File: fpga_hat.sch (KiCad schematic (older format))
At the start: 42 parts, among them IC1 ADV7125, IC3 CS4334, J0 0R, J1 0R, U1 AS6C4008-55PCN, U2 AS6C4008-55PCN, U7 Conn_02x32_Odd_Even, U8 Conn_02x32_Odd_Even

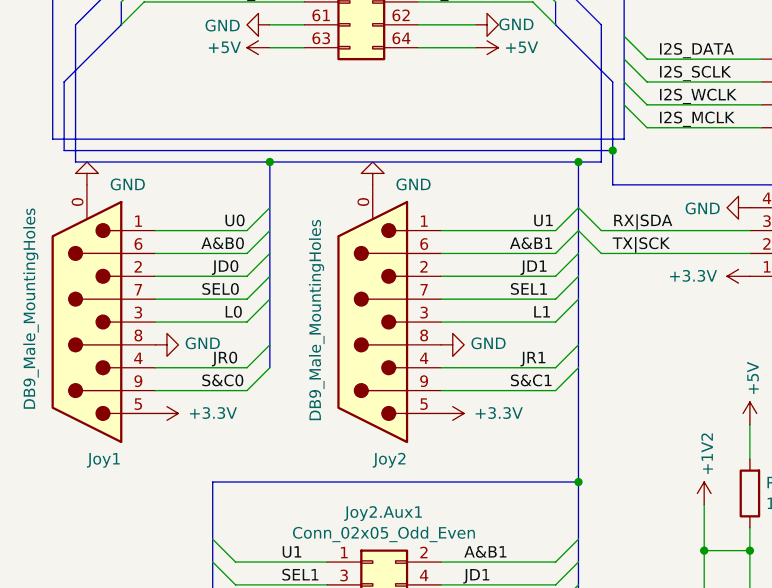
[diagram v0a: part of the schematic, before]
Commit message: Fixed gamepad port routing
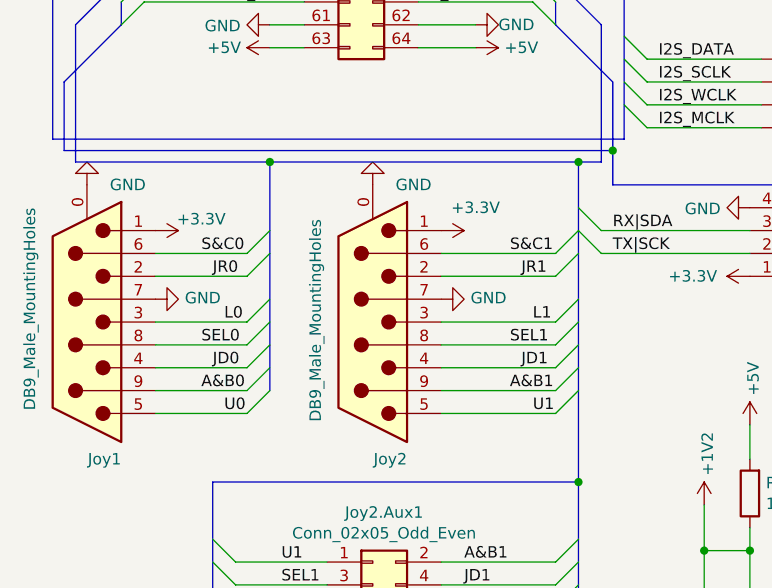
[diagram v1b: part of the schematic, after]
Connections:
- net +3V3: now also Joy1.1, Joy2.1; no longer Joy1.5, Joy2.5
- net A&B0: now also Joy1.9; no longer Joy1.6
- net A&B1: now also Joy2.9; no longer Joy2.6
- net GND: now also Joy1.7, Joy2.7; no longer Joy1.8, Joy2.8
- net JD0: now also Joy1.4; no longer Joy1.2
- net JD1: now also Joy2.4; no longer Joy2.2
- net JR0: now also Joy1.2; no longer Joy1.4
- net JR1: now also Joy2.2; no longer Joy2.4
- net S&C0: now also Joy1.6; no longer Joy1.9
- net S&C1: now also Joy2.6; no longer Joy2.9
- net SEL0: now also Joy1.8; no longer Joy1.7
- net SEL1: now also Joy2.8; no longer Joy2.7
- net U0: now also Joy1.5; no longer Joy1.1
- net U1: now also Joy2.5; no longer Joy2.1
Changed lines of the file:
@@
 Wire Wire Line
 	2300 4900 2550 4900
-$Comp
-L Connector:DB9_Male_MountingHoles Joy2
-U 1 1 6186E5CE
-P 2100 6200
-F 0 "Joy2" H 1950 6800 50  0000 L CNN
-F 1 "DB9_Male_MountingHoles" V 2350 5750 50  0000 L CNN
-F 2 "Connector_Dsub:DSUB-9_Female_Horizontal_P2.77x2.84mm_EdgePinOffset4.94mm_Housed_MountingHolesOffset7.48mm" H 2100 6200 50  0001 C CNN
-F 3 " ~" H 2100 6200 50  0001 C CNN
-	1    2100 6200
-	-1   0    0    1
-$EndComp
-Entry Wire Line
-	1550 5800 1650 5700
 Entry Wire Line
 	1550 5900 1650 5800
@@
 	1550 6000 1650 5900
 Entry Wire Line
-	1550 6100 1650 6000
+	1550 6300 1650 6200
 Entry Wire Line
 	1550 6200 1650 6100
@@
 	2900 6200 3000 6100
 Entry Wire Line
-	2900 6100 3000 6000
+	2900 6300 3000 6200
 Entry Wire Line
 	2900 6000 3000 5900
@@
 	2900 5900 3000 5800
 Entry Wire Line
-	2900 5800 3000 5700
-Wire Wire Line
-	1150 5800 1550 5800
+	2900 6600 3000 6500
 Wire Wire Line
 	1150 5900 1550 5900
@@
 	1150 6000 1550 6000
 Wire Wire Line
-	1150 6100 1550 6100
-Wire Wire Line
 	1150 6400 1550 6400
 Wire Wire Line
@@
 	2400 6200 2900 6200
 Wire Wire Line
-	2400 6100 2900 6100
-Wire Wire Line
 	2400 6000 2900 6000
 Wire Wire Line
 	2400 5900 2900 5900
-Wire Wire Line
-	2400 5800 2900 5800
-$Comp
-L power:GND #PWR0147
-U 1 1 61FF5750
-P 2400 6300
-F 0 "#PWR0147" H 2400 6050 50  0001 C CNN
-F 1 "GND" V 2405 6172 50  0000 R CNN
-F 2 "" H 2400 6300 50  0001 C CNN
-F 3 "" H 2400 6300 50  0001 C CNN
-	1    2400 6300
-	0    -1   -1   0
-$EndComp
 $Comp
 L power:GND #PWR0148
 U 1 1 61FF6E90
-P 1150 6300
-F 0 "#PWR0148" H 1150 6050 50  0001 C CNN
-F 1 "GND" V 1155 6172 50  0000 R CNN
-F 2 "" H 1150 6300 50  0001 C CNN
-F 3 "" H 1150 6300 50  0001 C CNN
-	1    1150 6300
+P 1150 6100
+F 0 "#PWR0148" H 1150 5850 50  0001 C CNN
+F 1 "GND" V 1155 5972 50  0000 R CNN
+F 2 "" H 1150 6100 50  0001 C CNN
+F 3 "" H 1150 6100 50  0001 C CNN
+	1    1150 6100
 	0    -1   -1   0
 $EndComp
@@
 L power:+3.3V #PWR0149
 U 1 1 61FF7B78
-P 1150 6600
-F 0 "#PWR0149" H 1150 6450 50  0001 C CNN
-F 1 "+3.3V" V 1150 6850 50  0000 C CNN
-F 2 "" H 1150 6600 50  0001 C CNN
-F 3 "" H 1150 6600 50  0001 C CNN
-	1    1150 6600
+P 1150 5800
+F 0 "#PWR0149" H 1150 5650 50  0001 C CNN
+F 1 "+3.3V" V 1100 6000 50  0000 C CNN
+F 2 "" H 1150 5800 50  0001 C CNN
+F 3 "" H 1150 5800 50  0001 C CNN
+	1    1150 5800
 	0    1    1    0
 $EndComp
@@
 L power:+3.3V #PWR0150
 U 1 1 62032B19
-P 2400 6600
-F 0 "#PWR0150" H 2400 6450 50  0001 C CNN
-F 1 "+3.3V" V 2400 6850 50  0000 C CNN
-F 2 "" H 2400 6600 50  0001 C CNN
-F 3 "" H 2400 6600 50  0001 C CNN
-	1    2400 6600
+P 2400 5800
+F 0 "#PWR0150" H 2400 5650 50  0001 C CNN
+F 1 "+3.3V" V 2300 5950 50  0000 C CNN
+F 2 "" H 2400 5800 50  0001 C CNN
+F 3 "" H 2400 5800 50  0001 C CNN
+	1    2400 5800
 	0    1    1    0
 $EndComp
 Connection ~ 1650 5500
-Text Label 1450 5800 0    50   ~ 0
+Text Label 1450 6600 0    50   ~ 0
 U0
-Text Label 1400 6000 0    50   ~ 0
+Text Label 1400 6400 0    50   ~ 0
 JD0
 Text Label 1450 6200 0    50   ~ 0
 L0
-Text Label 1400 6400 0    50   ~ 0
+Text Label 1400 6000 0    50   ~ 0
 JR0
+Text Label 1350 6500 0    50   ~ 0
+A&B0
+Text Label 1350 6300 0    50   ~ 0
+SEL0
 Text Label 1350 5900 0    50   ~ 0
-A&B0
-Text Label 1350 6100 0    50   ~ 0
-SEL0
-Text Label 1350 6500 0    50   ~ 0
 S&C0
-Text Label 2800 5800 0    50   ~ 0
+Text Label 2800 6600 0    50   ~ 0
 U1
-Text Label 2700 5900 0    50   ~ 0
-A&B1
-Text Label 2750 6000 0    50   ~ 0
+Text Label 2750 6400 0    50   ~ 0
 JD1
-Text Label 2700 6100 0    50   ~ 0
-SEL1
 Text Label 2800 6200 0    50   ~ 0
 L1
-Text Label 2750 6400 0    50   ~ 0
+Text Label 2750 6000 0    50   ~ 0
 JR1
-Text Label 2700 6500 0    50   ~ 0
-S&C1
 $Comp
 L Connector:Conn_01x04_Male Serial1
@@
 Wire Wire Line
 	3000 10100 3000 9950
-Wire Bus Line
-	9800 4800 9800 9150
-Wire Bus Line
-	1400 6900 1400 7450
-Wire Bus Line
-	3200 4150 3200 5400
-Wire Bus Line
-	3000 6900 3000 7450
-Wire Bus Line
-	4750 9150 9800 9150
-Wire Bus Line
-	2900 4000 2900 4700
-Wire Bus Line
-	1000 4000 1000 4700
-Wire Bus Line
-	1650 5500 1650 6400
-Wire Bus Line
-	8750 3700 8750 4800
-Wire Bus Line
-	6700 3700 6700 4800
-Wire Bus Line
-	4750 5600 6150 5600
-Wire Bus Line
-	4350 1050 4350 2900
-Wire Bus Line
-	3000 5500 3000 6900
-Wire Bus Line
-	8750 1050 8750 3400
-Wire Bus Line
-	1000 1050 1000 3500
-Wire Bus Line
-	4750 5600 4750 9150
-Wire Bus Line
-	6700 1050 6700 3400
-Wire Bus Line
-	2900 1050 2900 3500
-Wire Bus Line
-	5250 1050 5250 3500
 Connection ~ 3000 9950
 Wire Wire Line
@@
 Text GLabel 9400 7700 2    50   Input ~ 0
 AOUTJR
+Text Label 2700 6300 0    50   ~ 0
+SEL1
+Text Label 2700 6500 0    50   ~ 0
+A&B1
+Text Label 2700 5900 0    50   ~ 0
+S&C1
+Wire Wire Line
+	2900 6300 2400 6300
+Wire Wire Line
+	2900 6600 2400 6600
+$Comp
+L power:GND #PWR0147
+U 1 1 61FF5750
+P 2400 6100
+F 0 "#PWR0147" H 2400 5850 50  0001 C CNN
+F 1 "GND" V 2405 5972 50  0000 R CNN
+F 2 "" H 2400 6100 50  0001 C CNN
+F 3 "" H 2400 6100 50  0001 C CNN
+	1    2400 6100
+	0    -1   -1   0
+$EndComp
+$Comp
+L Connector:DB9_Male_MountingHoles Joy2
+U 1 1 6186E5CE
+P 2100 6200
+F 0 "Joy2" H 1950 6800 50  0000 L CNN
+F 1 "DB9_Male_MountingHoles" V 2350 5750 50  0000 L CNN
+F 2 "Connector_Dsub:DSUB-9_Female_Horizontal_P2.77x2.84mm_EdgePinOffset4.94mm_Housed_MountingHolesOffset7.48mm" H 2100 6200 50  0001 C CNN
+F 3 " ~" H 2100 6200 50  0001 C CNN
+	1    2100 6200
+	-1   0    0    1
+$EndComp
+Wire Wire Line
+	1150 6300 1550 6300
+Entry Wire Line
+	1550 6600 1650 6500
+Wire Wire Line
+	1150 6600 1550 6600
+Wire Bus Line
+	9800 4800 9800 9150
+Wire Bus Line
+	1400 6900 1400 7450
+Wire Bus Line
+	3000 6900 3000 7450
+Wire Bus Line
+	3200 4150 3200 5400
+Wire Bus Line
+	4750 9150 9800 9150
+Wire Bus Line
+	2900 4000 2900 4700
+Wire Bus Line
+	1000 4000 1000 4700
+Wire Bus Line
+	1650 5500 1650 6500
+Wire Bus Line
+	3000 5500 3000 6900
+Wire Bus Line
+	8750 3700 8750 4800
+Wire Bus Line
+	6700 3700 6700 4800
+Wire Bus Line
+	4750 5600 6150 5600
+Wire Bus Line
+	4350 1050 4350 2900
+Wire Bus Line
+	8750 1050 8750 3400
+Wire Bus Line
+	1000 1050 1000 3500
+Wire Bus Line
+	4750 5600 4750 9150
+Wire Bus Line
+	6700 1050 6700 3400
+Wire Bus Line
+	2900 1050 2900 3500
+Wire Bus Line
+	5250 1050 5250 3500
 $EndSCHEMATC
